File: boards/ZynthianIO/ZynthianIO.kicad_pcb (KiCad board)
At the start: 2 copper layers, 78.7 x 78.2 mm, 29 parts, among them J2 Raspberry_Pi_2_3, J3 GPIO, U1 MCP23017_SP, U2 6N138, U3 74LS14

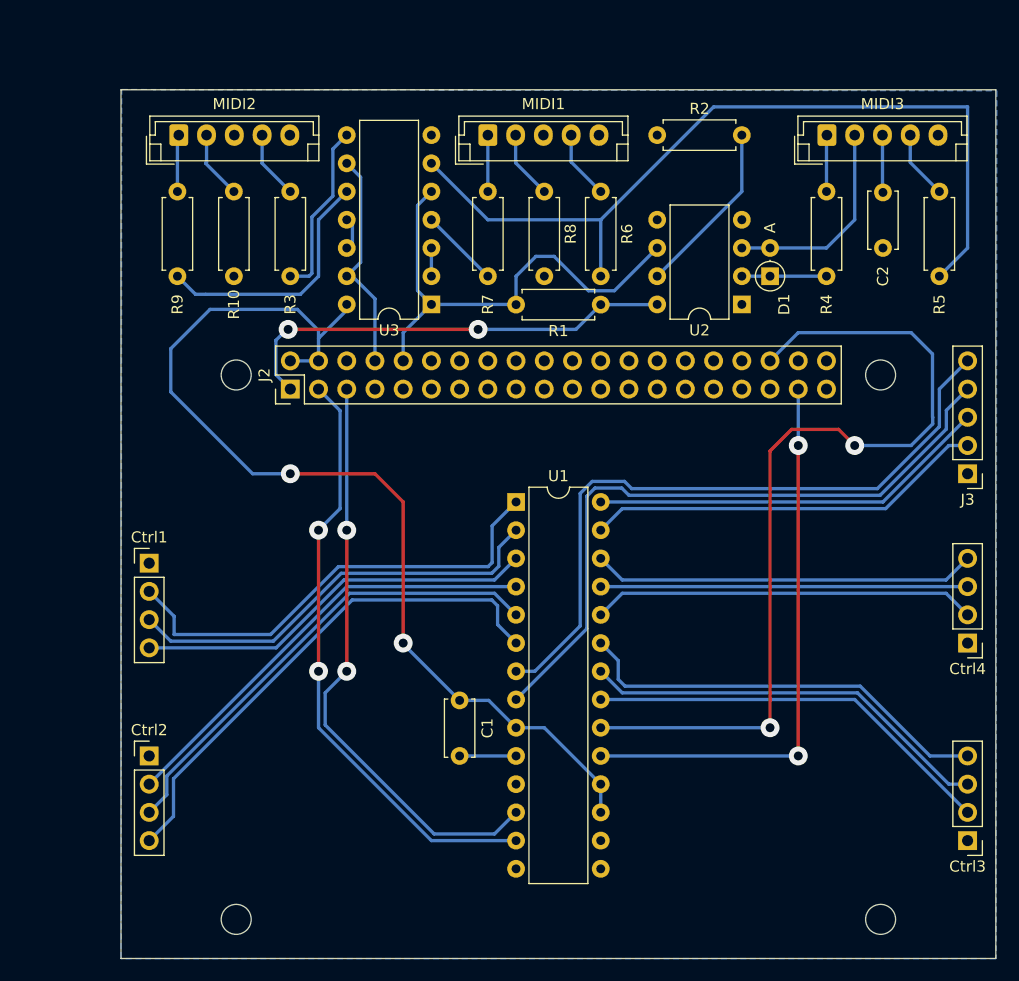
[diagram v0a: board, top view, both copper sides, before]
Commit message: New ZynthianIO board design for Boutique case
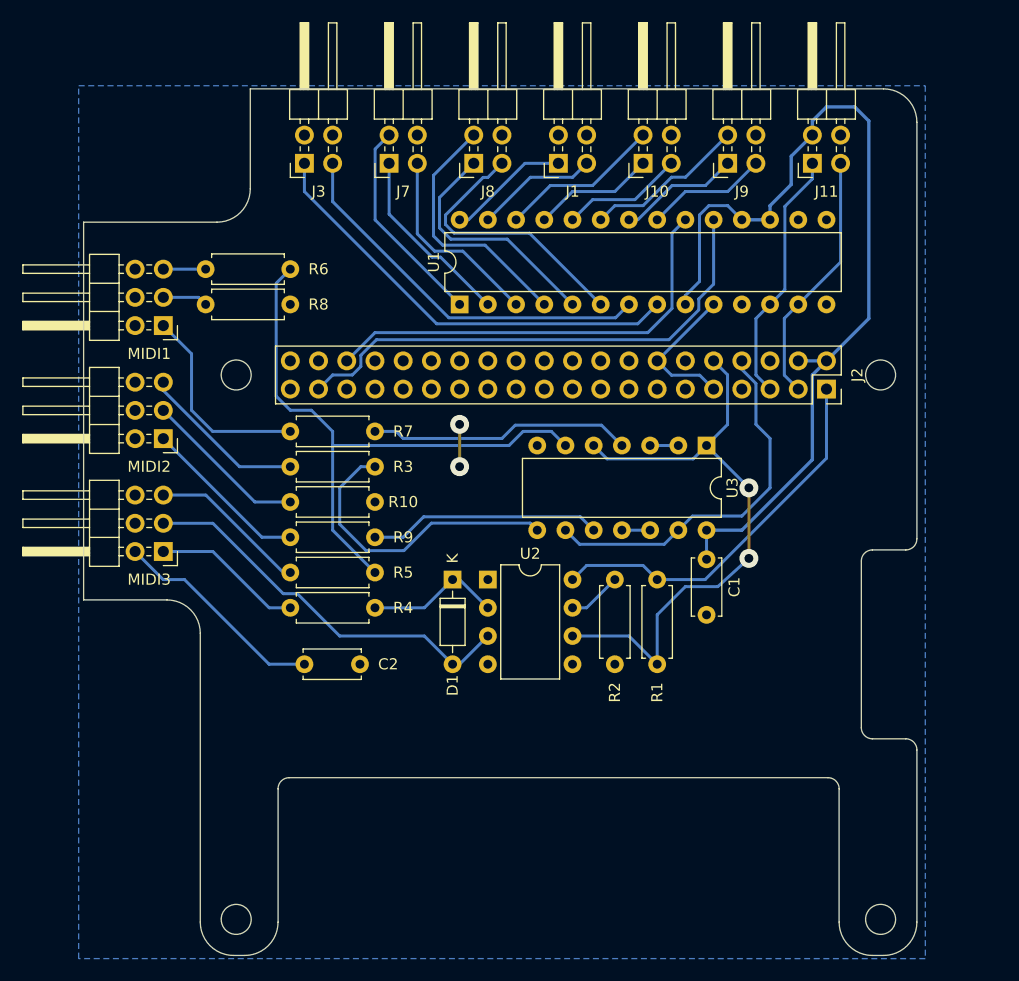
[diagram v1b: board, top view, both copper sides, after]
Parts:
- removed Ctrl1: Ctrl-3, Connector_PinHeader_2.54mm:PinHeader_1x04_P2.54mm_Vertical
- removed Ctrl2: Ctrl-4, Connector_PinHeader_2.54mm:PinHeader_1x04_P2.54mm_Vertical
- removed Ctrl3: Ctrl-1, Connector_PinHeader_2.54mm:PinHeader_1x04_P2.54mm_Vertical
- removed Ctrl4: Ctrl-2, Connector_PinHeader_2.54mm:PinHeader_1x04_P2.54mm_Vertical
- added J1: Btn-1, Connector_PinHeader_2.54mm:PinHeader_2x02_P2.54mm_Horizontal, F.Cu at (192.8, 80.1)
- added J10: Ctrl-2, Connector_PinHeader_2.54mm:PinHeader_2x02_P2.54mm_Horizontal, F.Cu at (200.5, 80.1)
- added J11: Display, Connector_PinHeader_2.54mm:PinHeader_2x02_P2.54mm_Horizontal, F.Cu at (215.7, 80.1)
- added J7: Ctrl-3, Connector_PinHeader_2.54mm:PinHeader_2x02_P2.54mm_Horizontal, F.Cu at (177.6, 80.1)
- added J8: Ctrl-4, Connector_PinHeader_2.54mm:PinHeader_2x02_P2.54mm_Horizontal, F.Cu at (185.2, 80.1)
- added J9: Ctrl-1, Connector_PinHeader_2.54mm:PinHeader_2x02_P2.54mm_Horizontal, F.Cu at (208.1, 80.1)
- D1: footprint Diode_THT:D_DO-35_SOD27_P2.54mm_Vertical_AnodeUp -> Diode_THT:D_DO-35_SOD27_P7.62mm_Horizontal
- J2: footprint Connector_PinHeader_2.54mm:PinHeader_2x20_P2.54mm_Vertical -> Connector_PinSocket_2.54mm:PinSocket_2x20_P2.54mm_Vertical
- J3: value GPIO -> Btn-2; footprint Connector_PinHeader_2.54mm:PinHeader_1x05_P2.54mm_Vertical -> Connector_PinHeader_2.54mm:PinHeader_2x02_P2.54mm_Horizontal
- MIDI1, MIDI2, MIDI3: footprint Connector_JST:JST_EH_B5B-EH-A_1x05_P2.50mm_Vertical -> Connector_PinHeader_2.54mm:PinHeader_2x03_P2.54mm_Horizontal
- moved MIDI3 70.5 mm to (157.3, 115.1), turned to 180 degrees
- moved R5 67.7 mm to (168.7, 117.0), turned to 0 degrees
- moved C2 67.2 mm to (170.0, 125.2), turned to 0 degrees
- moved J3 65.9 mm to (170.0, 80.1), turned to 90 degrees
- moved R4 61.1 mm to (168.7, 120.1), turned to 0 degrees
- moved J2 48.3 mm to (217.0, 100.4), turned to -90 degrees
- moved R2 47.8 mm to (197.9, 125.2), turned to 90 degrees
- moved D1 39.5 mm to (183.3, 117.6), turned to -90 degrees
- moved R6 36.2 mm to (161.1, 89.7), turned to 0 degrees
- moved MIDI1 33.9 mm to (157.3, 94.7), turned to 180 degrees
- moved U2 33.7 mm to (186.5, 117.6), turned to 0 degrees
- moved R9 32.7 mm to (168.7, 113.8), turned to 0 degrees
- moved R8 32.1 mm to (161.1, 92.8), turned to 0 degrees
- moved R10 28.4 mm to (168.7, 110.6), turned to 0 degrees
- moved R7 28.0 mm to (168.7, 104.3), turned to 0 degrees
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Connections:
- C2 pad 1: Net-(MIDI3-Pin_3) -> Net-(MIDI3-Pin_2)
- J2 pad 20: GND -> unconnected-(J2-GND-Pad20)
- J2 pad 30: GND -> unconnected-(J2-GND-Pad30)
- J2 pad 34: GND -> unconnected-(J2-GND-Pad34)
- J2 pad 6: unconnected-(J2-GND-Pad6) -> GND
- J3 pad 1: GND -> /GPB7
- J3 pad 2: /GPA6 -> GND
- J3 pad 3: /GPA7 -> /GPB6
- J3 pad 4: /GPB7 -> GND
- MIDI1 pad 2: Net-(MIDI1-Pin_2) -> GND
- MIDI1 pad 3: GND -> Net-(MIDI1-Pin_3)
- MIDI1 pad 4: Net-(MIDI1-Pin_4) -> GND
- MIDI1 pad 5: GND -> Net-(MIDI1-Pin_5)
- MIDI2 pad 2: Net-(MIDI2-Pin_2) -> GND
- MIDI2 pad 3: GND -> Net-(MIDI2-Pin_3)
- MIDI2 pad 4: Net-(MIDI2-Pin_4) -> GND
- MIDI2 pad 5: GND -> Net-(MIDI2-Pin_5)
- MIDI3 pad 2: Net-(D1-A) -> Net-(MIDI3-Pin_2)
- MIDI3 pad 3: Net-(MIDI3-Pin_3) -> Net-(D1-A)
- MIDI3 pad 4: Net-(MIDI3-Pin_4) -> GND
- MIDI3 pad 5: GND -> Net-(MIDI3-Pin_5)
- R10 pad 1: Net-(MIDI2-Pin_2) -> Net-(MIDI2-Pin_3)
- R3 pad 1: Net-(MIDI2-Pin_4) -> Net-(MIDI2-Pin_5)
- R5 pad 1: Net-(MIDI3-Pin_4) -> Net-(MIDI3-Pin_5)
- R6 pad 1: Net-(MIDI1-Pin_4) -> Net-(MIDI1-Pin_5)
- R8 pad 1: Net-(MIDI1-Pin_2) -> Net-(MIDI1-Pin_3)
- U1 pad 1: Net-(Ctrl1-Pin_2) -> /GPB0
- U1 pad 2: Net-(Ctrl1-Pin_3) -> /GPB1
- U1 pad 21: Net-(Ctrl3-Pin_2) -> /GPA0
- U1 pad 22: Net-(Ctrl3-Pin_3) -> /GPA1
- U1 pad 23: Net-(Ctrl3-Pin_4) -> /GPA2
- U1 pad 24: Net-(Ctrl4-Pin_2) -> /GPA3
- U1 pad 25: Net-(Ctrl4-Pin_3) -> /GPA4
- U1 pad 26: Net-(Ctrl4-Pin_4) -> /GPA5
- U1 pad 3: Net-(Ctrl1-Pin_4) -> /GPB2
- U1 pad 4: Net-(Ctrl2-Pin_2) -> /GPB3
- U1 pad 5: Net-(Ctrl2-Pin_3) -> /GPB4
- U1 pad 6: Net-(Ctrl2-Pin_4) -> /GPB5
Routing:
- net Net-(Ctrl2-Pin_4): track 46.6 -> 0.00 mm
- net Net-(Ctrl2-Pin_3): track 43.0 -> 0.00 mm
- net Net-(Ctrl1-Pin_2): track 42.5 -> 0.00 mm
- net Net-(Ctrl2-Pin_2): track 40.4 -> 0.00 mm
- net /INTA: track 79.8 -> 39.7 mm, vias 2 -> 0
- net Net-(Ctrl1-Pin_3): track 39.0 -> 0.00 mm
- net Net-(Ctrl3-Pin_4): track 38.2 -> 0.00 mm
- net Net-(Ctrl3-Pin_3): track 37.2 -> 0.00 mm
- net Net-(Ctrl3-Pin_2): track 37.2 -> 0.00 mm
- net Net-(Ctrl1-Pin_4): track 36.4 -> 0.00 mm
- net Net-(Ctrl4-Pin_4): track 34.6 -> 0.00 mm
- net Net-(Ctrl4-Pin_2): track 34.6 -> 0.00 mm
- net Net-(Ctrl4-Pin_3): track 33.0 -> 0.00 mm
- net /SDA: track 54.1 -> 22.9 mm, vias 2 -> 0
- net /SCK: track 53.1 -> 23.0 mm, vias 2 -> 0
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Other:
- board size 78.7 x 78.2 mm -> 75 x 78 mm

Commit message: Fixed MIDI interfaces
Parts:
- removed R2: 220, Resistor_THT:R_Axial_DIN0207_L6.3mm_D2.5mm_P7.62mm_Horizontal
- R1: value 220 -> 2k2
- R10, R4, R7, R8, R9: value 100 -> 220
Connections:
- R10 pad 2: GND -> Net-(R10-Pad2)
- R7 pad 2: Net-(R7-Pad2) -> +5V
- R8 pad 2: GND -> Net-(R8-Pad2)
- R9 pad 2: Net-(R9-Pad2) -> +5V
- U2 pad 7: Net-(U2-VO1) -> unconnected-(U2-VO1-Pad7)
- U3 pad 10: Net-(R9-Pad2) -> Net-(R10-Pad2)
- U3 pad 4: Net-(R7-Pad2) -> Net-(R8-Pad2)
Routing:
- net +5V: track 82.3 -> 124.1 mm
- net Net-(R8-Pad2): track 0.00 -> 40.6 mm
- net Net-(R7-Pad2): track 23.7 -> 0.00 mm
- net Net-(R9-Pad2): track 20.9 -> 0.00 mm
- net Net-(R10-Pad2): track 0.00 -> 20.7 mm
- net Net-(R3-Pad2): track 27.3 -> 21.0 mm
- net Net-(U2-VO1): track 4.86 -> 0.00 mm
- net Net-(R5-Pad2): track 54.6 -> 56.4 mm

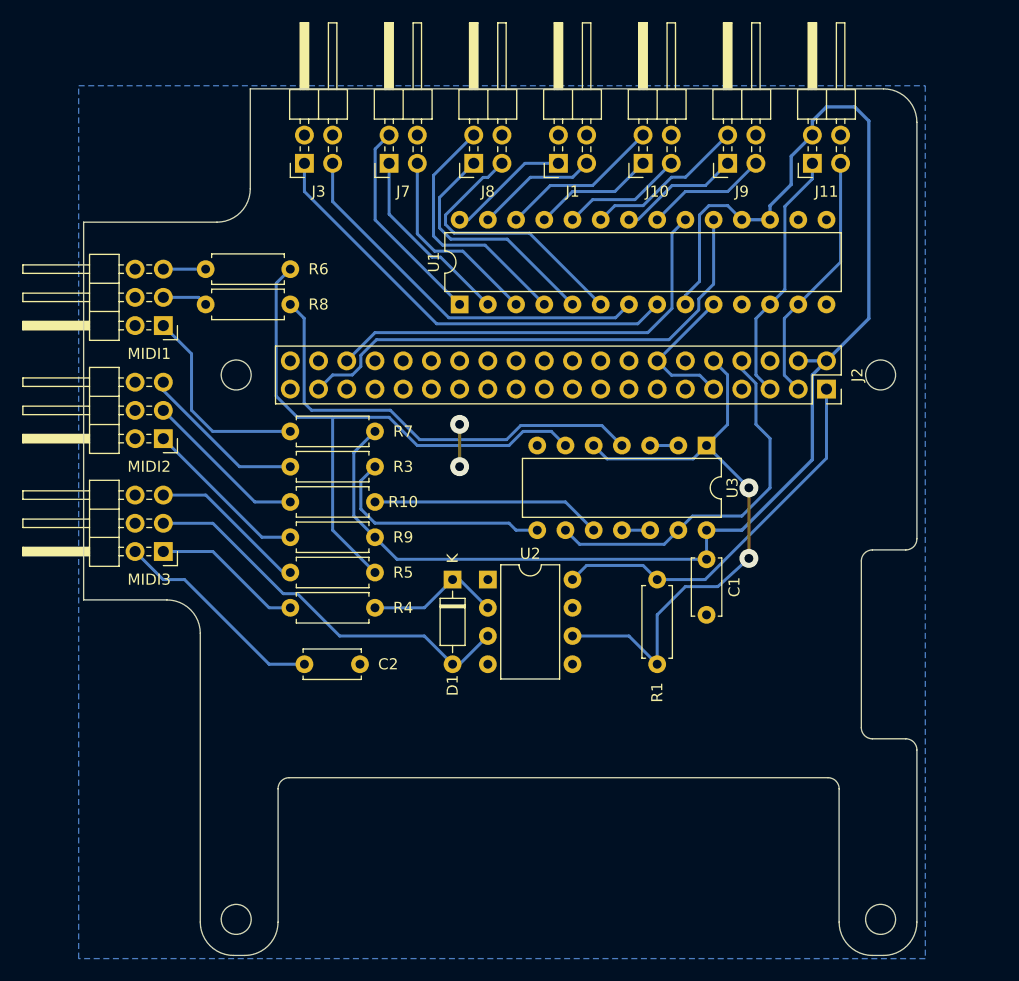
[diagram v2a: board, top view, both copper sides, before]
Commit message: Updated to KiCAD 8, use H11L1 as optocoupler
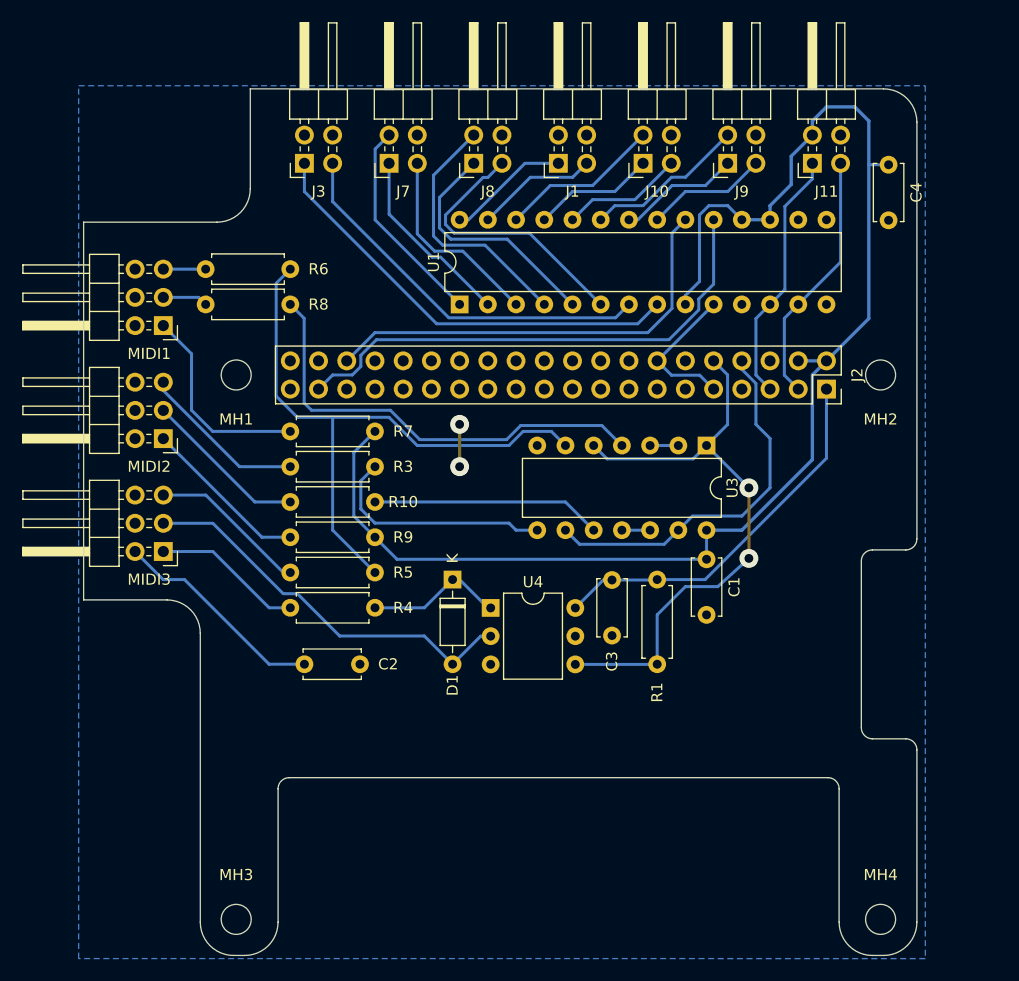
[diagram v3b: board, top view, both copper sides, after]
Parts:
- removed U2: 6N138, Package_DIP:DIP-8_W7.62mm
- added C3: 100n, Capacitor_THT:C_Disc_D5.0mm_W2.5mm_P5.00mm, F.Cu at (197.7, 117.6)
- added C4: 100n, Capacitor_THT:C_Disc_D5.0mm_W2.5mm_P5.00mm, F.Cu at (222.6, 80.3)
- added U4: H11L1, Package_DIP:DIP-6_W7.62mm, F.Cu at (186.7, 120.1)
- R1: value 2k2 -> 470
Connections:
- J2 pad 17: unconnected-(J2-3V3-Pad17) -> +3.3V
- J2 pad 20: unconnected-(J2-GND-Pad20) -> GND
- J2 pad 30: unconnected-(J2-GND-Pad30) -> GND
- J2 pad 34: unconnected-(J2-GND-Pad34) -> GND
- J2 pad 39: unconnected-(J2-GND-Pad39) -> GND
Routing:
- net +5V: track 124.1 -> 126.4 mm
- net /MIDI_IN: track 55.2 -> 53.9 mm
- net Net-(D1-A): track 34.9 -> 35.8 mm
